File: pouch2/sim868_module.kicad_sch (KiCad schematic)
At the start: 0 parts

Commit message: started routing
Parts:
- added U901: SIM868, SIM868:XCVR_SIM868, symbol SIM868:SIM868
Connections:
- new net: U901.13 (GND), U901.19 (GND), U901.21 (GND), U901.27 (GND), U901.30 (GND), U901.31 (GND), U901.33 (GND), U901.36 (GND), U901.37 (GND), U901.45 (GND), U901.63 (GND), U901.66 (GND), U901.67 (GND), U901.69 (GND), U901.70 (GND), U901.71 (GND), U901.72 (GND), U901.73 (GND), U901.74 (GND), U901.75 (GND), U901.76 (GND), U901.77 (GND), U901.8 (GND)
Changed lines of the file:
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@@
 		(comment 2 "Author: Leon Schnieber")
 	)
+	(symbol
+		(lib_id "SIM868:SIM868")
+		(at 134.62 87.63 0)
+		(unit 1)
+		(exclude_from_sim no)
+		(in_bom yes)
+		(on_board yes)
+		(dnp no)
+		(fields_autoplaced yes)
+		(property "Reference" "U901"
+			(at 134.62 36.83 0)
+			(effects
+				(font
+					(size 1.27 1.27)
+				)
+			)
+		)
+		(property "Value" "SIM868"
+			(at 134.62 39.37 0)
+			(effects
+				(font
+					(size 1.27 1.27)
+				)
+			)
+		)
+		(property "Footprint" "SIM868:XCVR_SIM868"
+			(at 134.62 87.63 0)
+			(effects
+				(font
+					(size 1.27 1.27)
+				)
+				(justify left bottom)
+				(hide yes)
+			)
+		)
+		(property "Datasheet" ""
+			(at 134.62 87.63 0)
+			(effects
+				(font
+					(size 1.27 1.27)
+				)
+				(justify left bottom)
+				(hide yes)
+			)
+		)
+		(property "Description" ""
+			(at 134.62 87.63 0)
+			(effects
+				(font
+					(size 1.27 1.27)
+				)
+				(hide yes)
+			)
+		)
+		(property "MANUFACTURER" "SimCom"
+			(at 134.62 87.63 0)
+			(effects
+				(font
+					(size 1.27 1.27)
+				)
+				(justify left bottom)
+				(hide yes)
+			)
+		)
+		(pin "30"
+		)
+		(pin "48"
+		)
+		(pin "26"
+		)
+		(pin "73"
+		)
+		(pin "16"
+		)
+		(pin "31"
+		)
+		(pin "55"
+		)
+		(pin "15"
+		)
+		(pin "22"
+		)
+		(pin "37"
+		)
+		(pin "17"
+		)
+		(pin "70"
+		)
+		(pin "66"
+		)
+		(pin "25"
+		)
+		(pin "11"
+		)
+		(pin "3"
+		)
+		(pin "60"
+		)
+		(pin "12"
+		)
+		(pin "41"
+		)
+		(pin "40"
+		)
+		(pin "20"
+		)
+		(pin "1"
+		)
+		(pin "68"
+		)
+		(pin "69"
+		)
+		(pin "2"
+		)
+		(pin "14"
+		)
+		(pin "59"
+		)
+		(pin "36"
+		)
+		(pin "63"
+		)
+		(pin "76"
+		)
+		(pin "35"
+		)
+		(pin "58"
+		)
+		(pin "51"
+		)
+		(pin "8"
+		)
+		(pin "54"
+		)
+		(pin "21"
+		)
+		(pin "61"
+		)
+		(pin "5"
+		)
+		(pin "23"
+		)
+		(pin "29"
+		)
+		(pin "19"
+		)
+		(pin "32"
+		)
+		(pin "75"
+		)
+		(pin "24"
+		)
+		(pin "56"
+		)
+		(pin "62"
+		)
+		(pin "42"
+		)
+		(pin "47"
+		)
+		(pin "10"
+		)
+		(pin "13"
+		)
+		(pin "27"
+		)
+		(pin "71"
+		)
+		(pin "38"
+		)
+		(pin "74"
+		)
+		(pin "52"
+		)
+		(pin "18"
+		)
+		(pin "45"
+		)
+		(pin "44"
+		)
+		(pin "4"
+		)
+		(pin "6"
+		)
+		(pin "46"
+		)
+		(pin "7"
+		)
+		(pin "77"
+		)
+		(pin "39"
+		)
+		(pin "33"
+		)
+		(pin "67"
+		)
+		(pin "28"
+		)
+		(pin "34"
+		)
+		(pin "64"
+		)
+		(pin "50"
+		)
+		(pin "57"
+		)
+		(pin "49"
+		)
+		(pin "65"
+		)
+		(pin "9"
+		)
+		(pin "53"
+		)
+		(pin "72"
+		)
+		(pin "43"
+		)
+		(instances
+			(project ""
+				(path "/278cfa6b-9496-4a22-b425-8abdb96793ef/c2c54002-cd4a-4798-8316-b28ab1c46cc6"
+					(reference "U901")
+					(unit 1)
+				)
+			)
+		)
+	)
 )

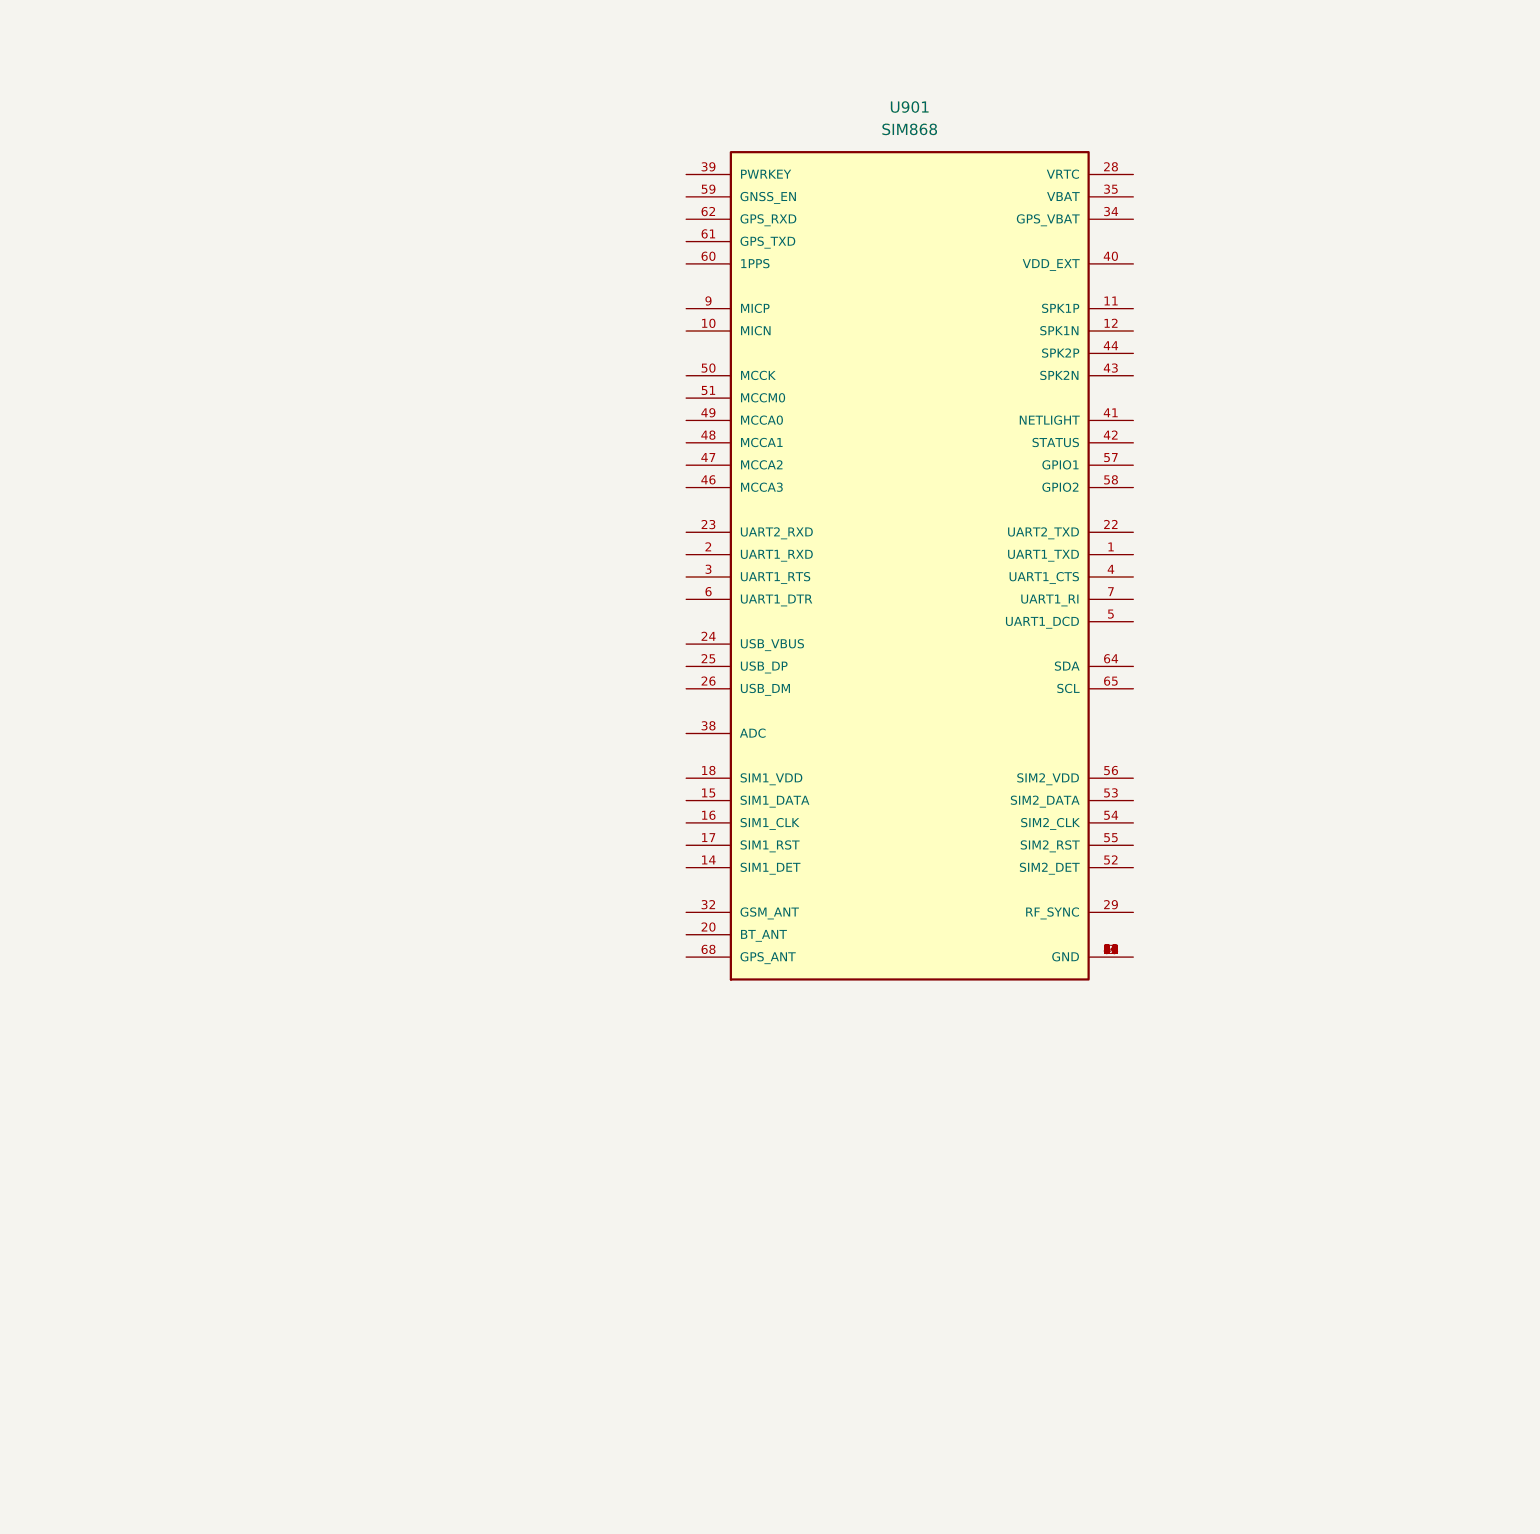
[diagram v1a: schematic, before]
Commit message: added sim-module breakout
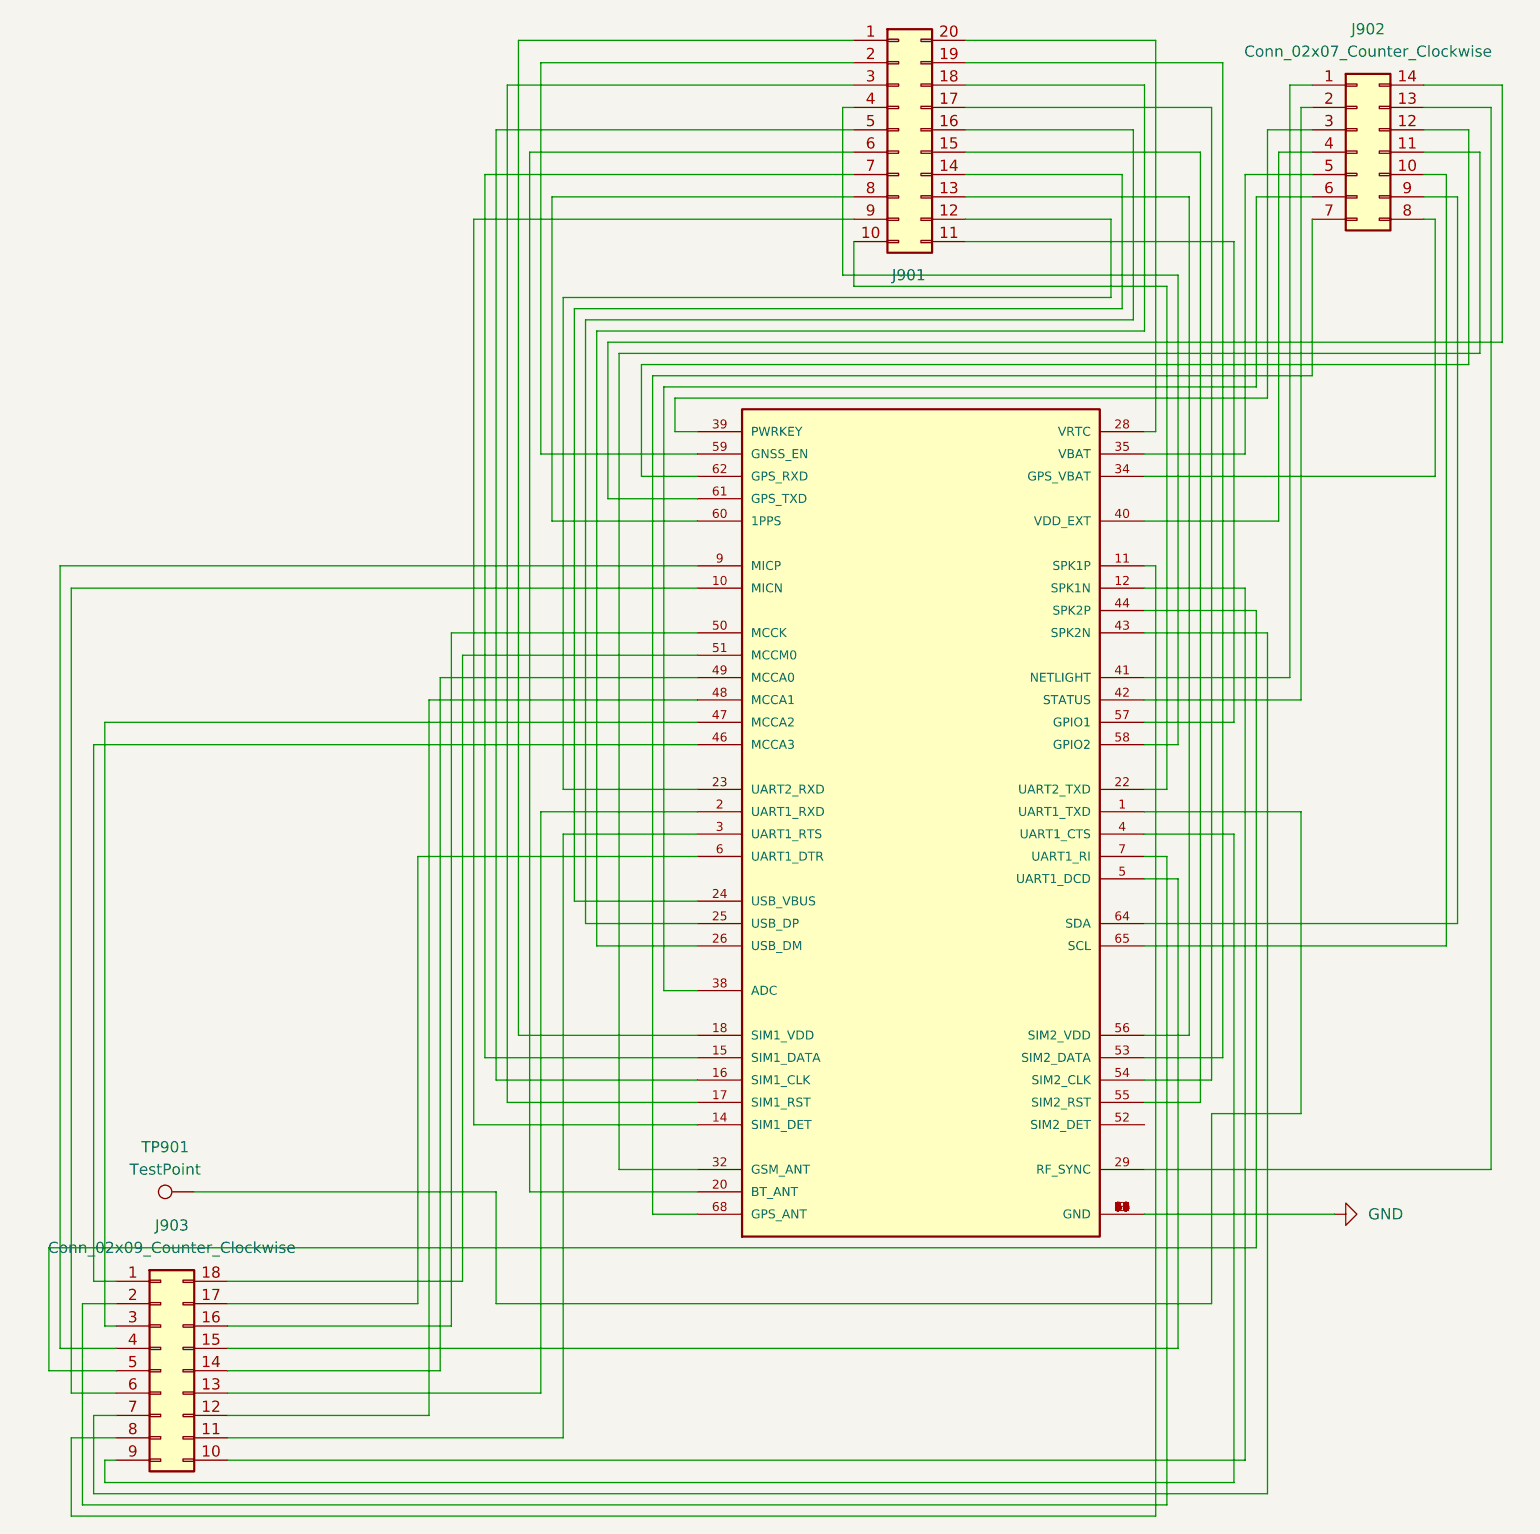
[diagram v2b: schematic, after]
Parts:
- added J901: Conn_02x03_Counter_Clockwise, Connector_PinHeader_1.00mm:PinHeader_2x10_P1.00mm_Vertical_SMD, symbol Connector_Generic:Conn_02x10_Counter_Clockwise
- added J902: Conn_02x07_Counter_Clockwise, Connector_PinHeader_1.00mm:PinHeader_2x07_P1.00mm_Vertical_SMD, symbol Connector_Generic:Conn_02x07_Counter_Clockwise
- added J903: Conn_02x09_Counter_Clockwise, Connector_PinHeader_1.00mm:PinHeader_2x09_P1.00mm_Vertical_SMD, symbol Connector_Generic:Conn_02x09_Counter_Clockwise
- added TP901: TestPoint, TestPoint:TestPoint_Pad_D1.0mm, symbol Connector:TestPoint
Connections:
- net at U901.1 (UART1_TXD): now also TP901.1
- net at U901.10 (MICN): now also J903.6 (Pin_6)
- net at U901.11 (SPK1P): now also J903.8 (Pin_8)
- net at U901.12 (SPK1N): now also J903.10 (Pin_10)
- net GND: now reaches U901.13 (GND), U901.19 (GND), U901.21 (GND), U901.27 (GND), U901.30 (GND), U901.31 (GND), U901.33 (GND), U901.36 (GND), U901.37 (GND), U901.45 (GND), U901.63 (GND), U901.66 (GND), U901.67 (GND), U901.69 (GND), U901.70 (GND), U901.71 (GND), U901.72 (GND), U901.73 (GND), U901.74 (GND), U901.75 (GND), U901.76 (GND), U901.77 (GND), U901.8 (GND)
- net at U901.14 (SIM1_DET): now also J901.9 (Pin_9)
- net at U901.15 (SIM1_DATA): now also J901.7 (Pin_7)
- net at U901.16 (SIM1_CLK): now also J901.5 (Pin_5)
- net at U901.17 (SIM1_RST): now also J901.3 (Pin_3)
- net at U901.18 (SIM1_VDD): now also J901.1 (Pin_1)
- net at U901.2 (UART1_RXD): now also J903.13 (Pin_13)
- net at U901.20 (BT_ANT): now also J901.6 (Pin_6)
- net at U901.22 (UART2_TXD): now also J901.10 (Pin_10)
- net at U901.23 (UART2_RXD): now also J901.12 (Pin_12)
- net at U901.24 (USB_VBUS): now also J901.14 (Pin_14)
- net at U901.25 (USB_DP): now also J901.16 (Pin_16)
- net at U901.26 (USB_DM): now also J901.18 (Pin_18)
- net at U901.28 (VRTC): now also J901.20 (Pin_20)
- net at U901.29 (RF_SYNC): now also J902.13 (Pin_13)
- net at U901.3 (UART1_RTS): now also J903.11 (Pin_11)
- net at U901.32 (GSM_ANT): now also J902.11 (Pin_11)
- net at U901.34 (GPS_VBAT): now also J902.8 (Pin_8)
- net at U901.35 (VBAT): now also J902.5 (Pin_5)
- net at U901.38 (ADC): now also J902.6 (Pin_6)
- net at U901.39 (PWRKEY): now also J902.3 (Pin_3)
- net at U901.4 (UART1_CTS): now also J903.9 (Pin_9)
- net at U901.40 (VDD_EXT): now also J902.4 (Pin_4)
- net at U901.41 (NETLIGHT): now also J902.1 (Pin_1)
- net at U901.42 (STATUS): now also J902.2 (Pin_2)
- net at U901.43 (SPK2N): now also J903.7 (Pin_7)
- net at U901.44 (SPK2P): now also J903.5 (Pin_5)
- net at U901.46 (MCCA3): now also J903.1 (Pin_1)
- net at U901.47 (MCCA2): now also J903.3 (Pin_3)
- net at U901.48 (MCCA1): now also J903.12 (Pin_12)
- net at U901.49 (MCCA0): now also J903.14 (Pin_14)
- net at U901.5 (UART1_DCD): now also J903.15 (Pin_15)
- net at U901.50 (MCCK): now also J903.16 (Pin_16)
- net at U901.51 (MCCM0): now also J903.18 (Pin_18)
- net at U901.53 (SIM2_DATA): now also J901.19 (Pin_19)
- net at U901.54 (SIM2_CLK): now also J901.17 (Pin_17)
- net at U901.55 (SIM2_RST): now also J901.15 (Pin_15)
- net at U901.56 (SIM2_VDD): now also J901.13 (Pin_13)
- net at U901.57 (GPIO1): now also J901.11 (Pin_11)
- net at U901.58 (GPIO2): now also J901.4 (Pin_4)
- net at U901.59 (GNSS_EN): now also J901.2 (Pin_2)
- net at U901.6 (UART1_DTR): now also J903.17 (Pin_17)
- net at U901.60 (1PPS): now also J901.8 (Pin_8)
- net at U901.61 (GPS_TXD): now also J902.14 (Pin_14)
- net at U901.62 (GPS_RXD): now also J902.12 (Pin_12)
- net at U901.64 (SDA): now also J902.9 (Pin_9)
- net at U901.65 (SCL): now also J902.10 (Pin_10)
- net at U901.68 (GPS_ANT): now also J902.7 (Pin_7)
- net at U901.7 (UART1_RI): now also J903.2 (Pin_2)
- net at U901.9 (MICP): now also J903.4 (Pin_4)

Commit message: rev1
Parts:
- J901, J902, J903, U901: OrderStatus (none) -> manual
- TP901: OrderStatus (none) -> dnp
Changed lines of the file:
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@@
+			)
+		)
+		(property "OrderStatus" "manual"
+			(at 185.42 41.91 0)
+			(effects
+				(font
+					(size 1.27 1.27)
+				)
+				(hide yes)
 			)
 		)
@@
 			)
 		)
+		(property "OrderStatus" "manual"
+			(at 49.53 180.34 0)
+			(effects
+				(font
+					(size 1.27 1.27)
+				)
+				(hide yes)
+			)
+		)
 		(pin "9"
 		)
@@
 			)
 		)
+		(property "OrderStatus" "manual"
+			(at 135.89 116.84 0)
+			(effects
+				(font
+					(size 1.27 1.27)
+				)
+				(hide yes)
+			)
+		)
 		(pin "30"
 		)
@@
 		)
 		(property "MPN_Eurocircuit" ""
+			(at 133.35 39.37 0)
+			(effects
+				(font
+					(size 1.27 1.27)
+				)
+				(hide yes)
+			)
+		)
+		(property "OrderStatus" "manual"
 			(at 133.35 39.37 0)
 			(effects
@@
 			(at 53.34 160.02 0)
 			(effects
+				(font
+					(size 1.27 1.27)
+				)
+				(hide yes)
+			)
+		)
+		(property "OrderStatus" "dnp"
+			(at 53.34 160.02 0)
+			(effects
